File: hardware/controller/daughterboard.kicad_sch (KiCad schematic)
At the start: 9 parts, among them J1 TYPE-C-31-D-06, J8 FPC_12P_0.5mm, SW89 SW_Push, SW91 SW_Push, U3 TPD4E05U06DQAR

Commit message: feat(controller): 1x10 MB-DB header, isolate DB nets, drop DB buttons and LEDs
J9 (MB) and J8 (DB) as Conn_01x10 with I1 pinout; DB nets renamed DB_*,
no hierarchical links between MB and DB sheets; SW89, SW91, D4, D92 removed.
Layout around J9 still to be tidied.

Co-Authored-By: Claude Opus 5.5 (1M context) <noreply@anthropic.com>
Claude-Session: https://claude.ai/code/session_011u4PgyeeXFvTvHcxLBDiHw
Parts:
- removed D4, D92: rgb, easyeda2kicad:WS2812C-2020-V1, symbol easyeda2kicad:rgb
- removed SW89, SW91: SW_Push, easyeda2kicad:KEY-SMD_B3U-1000PM, symbol Switch:SW_Push
- J8: value FPC_12P_0.5mm -> J_DB 1x10 P1.00mm; footprint easyeda2kicad:FPC_12P_0.5mm -> Connector_PinHeader_1.00mm:PinHeader_1x10_P1.00mm_Vertical_SMD_Pin1Left; symbol Connector_Generic:Conn_01x12 -> Connector_Generic:Conn_01x10
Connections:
- net GND is gone; now on net DB_GND: D1.1 (A1), J1.A1 (GND), J1.A12 (GND), J1.B1 (GND), J1.B12 (GND), J1.S1 (SHIELD), J8.5 (Pin_5), J8.8 (Pin_8), U3.3 (GND), U3.8 (GND)
- net LED_DATA is gone; now on net DB_GND: J8.10 (Pin_10)
- net BT_PAIR renamed DB_GND
- net CC1 renamed DB_CC1
- net CC2 renamed DB_CC2
- net D+ renamed DB_D+
- net D- renamed DB_D-
- removed net SHPHLD: J8.11 (Pin_11)
- net VBUS renamed DB_VBUS
- removed net VSYS: J8.12 (Pin_12)
- no-connect marks 3 -> 2

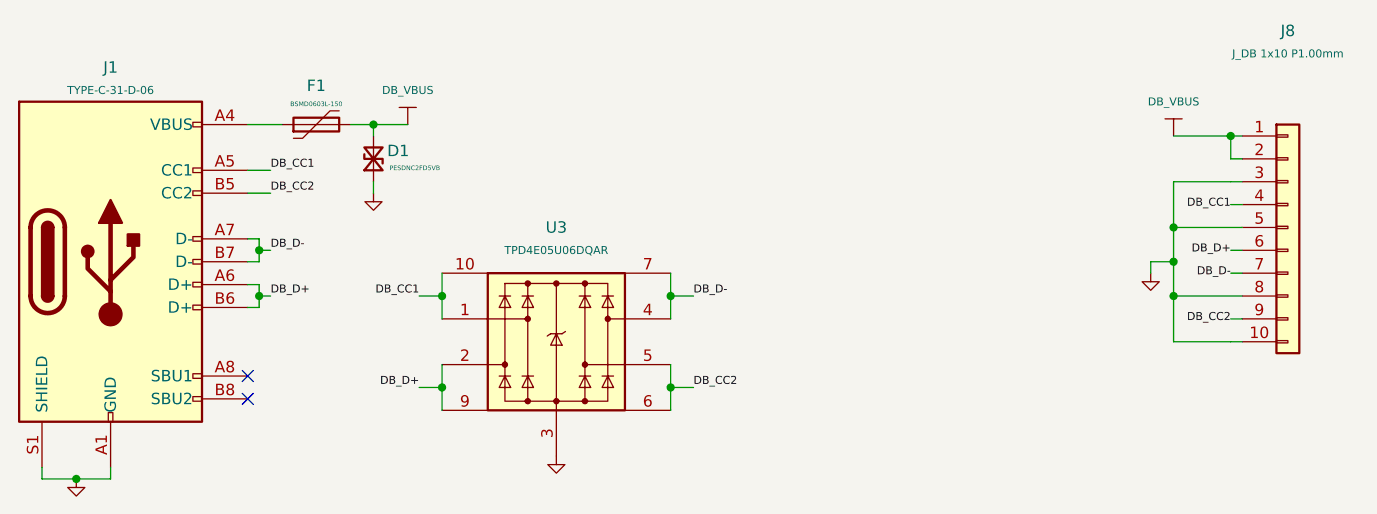
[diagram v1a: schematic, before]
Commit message: feat(controller): U2 on ibm_m nPM1300 symbol, PMIC step 1 (P1-P4, P7, P10)
BUCK2 drives VDD_NRF (L4 SW2-VOUT2, R10 470k on VSET2), BUCK1 terminated,
PVSS2 net-tie NT1 to GND, NTC to GND (TH1 removed), LSIN1 on VSYS,
VDDIO on VDD_NRF with C35 100n, GPIO0 PMIC_INT, GPIO1 LED_EN labels.

Co-Authored-By: Claude Opus 5.5 (1M context) <noreply@anthropic.com>
Claude-Session: https://claude.ai/code/session_011u4PgyeeXFvTvHcxLBDiHw
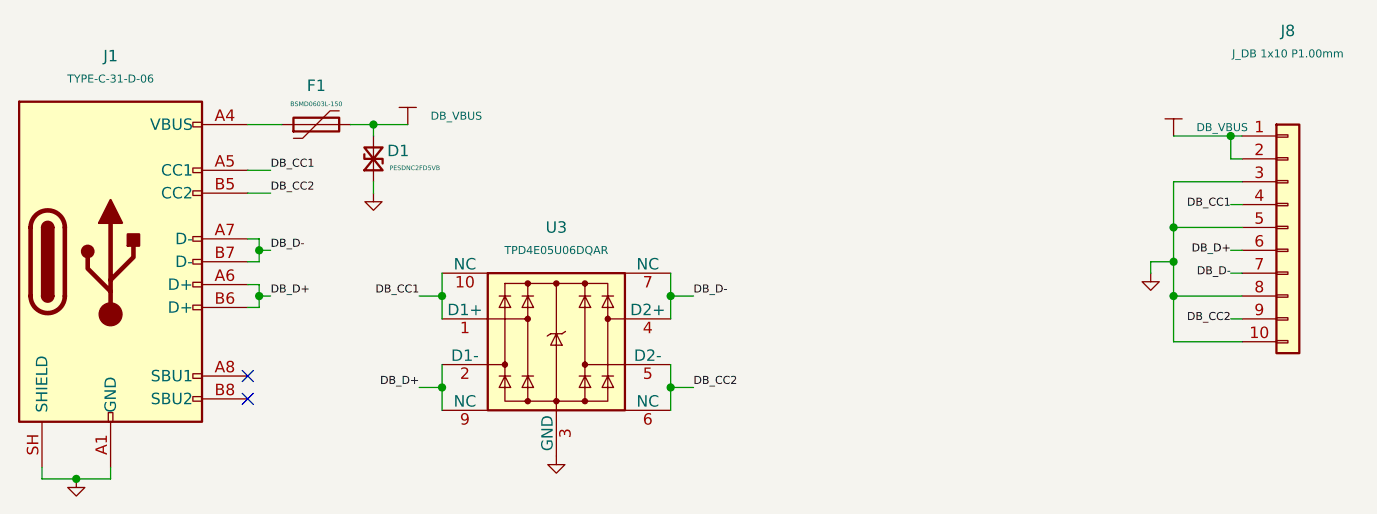
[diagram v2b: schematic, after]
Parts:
- D1: footprint easyeda2kicad:Diodes_DFN1006-2 -> (none); LCSC Part C110694 -> (none)
- F1: footprint Fuse:Fuse_0603_1608Metric -> (none); LCSC Part C914094 -> (none)
- J1: footprint easyeda2kicad:USB-C-SMD_TYPE-C-31-D-06 -> (none); LCSC Part C2689964 -> (none)
- J8: footprint Connector_PinHeader_1.00mm:PinHeader_1x10_P1.00mm_Vertical_SMD_Pin1Left -> (none); now in the parts list
- U3: LCSC Part C138714 -> (none)
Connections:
- net DB_GND: now also J1.SH (SHIELD); no longer J1.S1 (SHIELD)
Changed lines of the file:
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@@
+	)
+	(junction
+		(at 193.04 92.71)
+		(diameter 0)
+		(color 0 0 0 0)
+	)
+	(junction
+		(at 193.04 85.09)
+		(diameter 0)
+		(color 0 0 0 0)
 	)
 	(junction
@@
 	(wire
 		(pts
-			(xy 199.39 80.01) (xy 200.66 80.01)
+			(xy 193.04 80.01) (xy 200.66 80.01)
 		)
 		(stroke
@@
 	(wire
 		(pts
+			(xy 193.04 80.01) (xy 193.04 85.09)
+		)
+		(stroke
+			(width 0)
+			(type default)
+		)
+	)
+	(wire
+		(pts
 			(xy 200.66 77.47) (xy 199.39 77.47)
 		)
@@
 	(wire
 		(pts
+			(xy 193.04 92.71) (xy 193.04 97.79)
+		)
+		(stroke
+			(width 0)
+			(type default)
+		)
+	)
+	(wire
+		(pts
 			(xy 199.39 87.63) (xy 200.66 87.63)
 		)
@@
 	(wire
 		(pts
-			(xy 199.39 97.79) (xy 200.66 97.79)
-		)
-		(stroke
-			(width 0)
-			(type default)
-		)
-	)
-	(wire
-		(pts
 			(xy 101.6 73.66) (xy 104.14 73.66)
 		)
@@
 	(wire
 		(pts
+			(xy 193.04 97.79) (xy 200.66 97.79)
+		)
+		(stroke
+			(width 0)
+			(type default)
+		)
+	)
+	(wire
+		(pts
 			(xy 91.44 91.44) (xy 91.44 92.71)
 		)
@@
 			(width 0)
 			(type default)
+		)
+	)
+	(label "DB_CC2"
+		(at 199.39 95.25 180)
+		(effects
+			(font
+				(size 0.889 0.889)
+			)
+			(justify right)
+		)
+	)
+	(label "DB_D+"
+		(at 199.39 87.63 180)
+		(effects
+			(font
+				(size 0.889 0.889)
+			)
+			(justify right)
+		)
+	)
+	(label "DB_D-"
+		(at 199.39 90.17 180)
+		(effects
+			(font
+				(size 0.889 0.889)
+			)
+			(justify right)
+		)
+	)
+	(label "DB_CC1"
+		(at 199.39 82.55 180)
+		(effects
+			(font
+				(size 0.889 0.889)
+			)
+			(justify right)
 		)
 	)
@@
 			)
 			(justify left bottom)
-		)
-	)
-	(label "DB_CC2"
-		(at 199.39 95.25 180)
-		(effects
-			(font
-				(size 0.889 0.889)
-			)
-			(justify right)
-		)
-	)
-	(label "DB_D+"
-		(at 199.39 87.63 180)
-		(effects
-			(font
-				(size 0.889 0.889)
-			)
-			(justify right)
-		)
-	)
-	(label "DB_D-"
-		(at 199.39 90.17 180)
-		(effects
-			(font
-				(size 0.889 0.889)
-			)
-			(justify right)
-		)
-	)
-	(label "DB_CC1"
-		(at 199.39 82.55 180)
-		(effects
-			(font
-				(size 0.889 0.889)
-			)
-			(justify right)
 		)
 	)
@@
 			)
 		)
-		(property "Footprint" "Fuse:Fuse_0603_1608Metric"
+		(property "Footprint" ""
 			(at 102.87 72.39 0)
 			(hide yes)
@@
 			)
 		)
-		(property "Datasheet" "https://www.lcsc.com/product-detail/C914094.html"
+		(property "Datasheet" ""
 			(at 97.79 73.66 0)
 			(hide yes)
@@
 			)
 		)
-		(property "LCSC Part" "C914094"
-			(at 97.79 73.66 90)
-			(hide yes)
-			(show_name no)
-			(do_not_autoplace no)
-			(effects
-				(font
-					(size 1.27 1.27)
-				)
-			)
-		)
 		(pin "2"
 		)
@@
 		)
 		(instances
-			(project "ibm-modern-m-ssk"
+			(project "controller"
 				(path "/17f6a4a5-fbff-4e30-a1cc-9481373e4968/c9a46136-57a3-45fc-88ce-38da53378f82"
 					(reference "F1")
@@
 		)
 		(instances
-			(project "ibm-modern-m-ssk"
+			(project "controller"
 				(path "/17f6a4a5-fbff-4e30-a1cc-9481373e4968/c9a46136-57a3-45fc-88ce-38da53378f82"
 					(reference "#PWR037")
@@
 		(fields_autoplaced yes)
 		(property "Reference" "J1"
-			(at 74.93 67.31 0)
+			(at 74.93 66.04 0)
 			(show_name no)
 			(do_not_autoplace no)
@@
 		)
 		(property "Value" "TYPE-C-31-D-06"
-			(at 74.93 69.85 0)
+			(at 74.93 68.58 0)
 			(show_name no)
 			(do_not_autoplace no)
@@
 			)
 		)
-		(property "Footprint" "easyeda2kicad:USB-C-SMD_TYPE-C-31-D-06"
+		(property "Footprint" ""
 			(at 78.74 88.9 0)
 			(hide yes)
@@
 			)
 		)
-		(property "LCSC Part" "C2689964"
-			(at 74.93 88.9 0)
-			(hide yes)
-			(show_name no)
-			(do_not_autoplace no)
-			(effects
-				(font
-					(size 1.27 1.27)
-				)
-			)
-		)
-		(pin "S1"
+		(pin "SH"
 		)
 		(pin "B7"
@@
 		)
 		(instances
-			(project "ibm-modern-m-ssk"
+			(project "controller"
 				(path "/17f6a4a5-fbff-4e30-a1cc-9481373e4968/c9a46136-57a3-45fc-88ce-38da53378f82"
 					(reference "J1")
@@
 		(body_style 1)
 		(exclude_from_sim no)
-		(in_bom no)
+		(in_bom yes)
 		(on_board yes)
-		(in_pos_files no)
+		(in_pos_files yes)
 		(dnp no)
 		(property "Reference" "J8"
@@
 			)
 		)
-		(property "Footprint" "Connector_PinHeader_1.00mm:PinHeader_1x10_P1.00mm_Vertical_SMD_Pin1Left"
+		(property "Footprint" ""
 			(at 205.74 85.09 0)
 			(hide yes)
@@
 			)
 		)
-		(property "Datasheet" "~"
+		(property "Datasheet" ""
 			(at 205.74 85.09 0)
 			(hide yes)
@@
 			)
 		)
-		(property "Description" "Goldpin 1x10, raster 1,00 mm; lacze MB-DB, pinout wg I1: VBUS, VBUS, GND, CC1, GND, D+, D-, GND, CC2, GND. Strona DB: piny lutowane do krawedzi; footprint tymczasowy, poza BOM i CPL (czesc liczona przy J9)"
+		(property "Description" "Generic connector, single row, 01x10, script generated (kicad-library-utils/schlib/autogen/connector/)"
 			(at 205.74 85.09 0)
 			(hide yes)
@@
 			)
 		)
-		(property "LCSC Part" ""
-			(at 205.74 85.09 0)
-			(hide yes)
-			(show_name no)
-			(do_not_autoplace no)
-			(effects
-				(font
-					(size 1.27 1.27)
-				)
-			)
-		)
 		(pin "3"
 		)
@@
 		)
 		(instances
-			(project "ibm-modern-m-ssk"
+			(project "controller"
 				(path "/17f6a4a5-fbff-4e30-a1cc-9481373e4968/c9a46136-57a3-45fc-88ce-38da53378f82"
 					(reference "J8")
@@
 			)
 		)
-		(property "Footprint" "easyeda2kicad:Diodes_DFN1006-2"
+		(property "Footprint" ""
 			(at 104.14 77.47 0)
 			(hide yes)
@@
 			)
 		)
-		(property "Datasheet" "https://www.lcsc.com/product-detail/C110694.html"
+		(property "Datasheet" ""
 			(at 104.14 77.47 0)
 			(hide yes)
@@
 			)
 		)
-		(property "LCSC Part" "C110694"
-			(at 104.14 77.47 90)
-			(hide yes)
-			(show_name no)
-			(do_not_autoplace no)
-			(effects
-				(font
-					(size 1.27 1.27)
-				)
-			)
-		)
 		(pin "1"
 		)
@@
 		)
 		(instances
-			(project "ibm-modern-m-ssk"
+			(project "controller"
 				(path "/17f6a4a5-fbff-4e30-a1cc-9481373e4968/c9a46136-57a3-45fc-88ce-38da53378f82"
 					(reference "D1")
@@
 			)
 		)
-		(property "LCSC Part" "C138714"
-			(at 124.46 97.79 0)
-			(hide yes)
-			(show_name no)
-			(do_not_autoplace no)
-			(effects
-				(font
-					(size 1.27 1.27)
-				)
-			)
-		)
 		(pin "5"
 		)
@@
 		)
 		(instances
-			(project "ibm-modern-m-ssk"
+			(project "controller"
 				(path "/17f6a4a5-fbff-4e30-a1cc-9481373e4968/c9a46136-57a3-45fc-88ce-38da53378f82"
 					(reference "U3")
@@
 		)
 		(instances
-			(project "ibm-modern-m-ssk"
+			(project "controller"
 				(path "/17f6a4a5-fbff-4e30-a1cc-9481373e4968/c9a46136-57a3-45fc-88ce-38da53378f82"
 					(reference "#PWR038")
@@
 		)
 		(property "Value" "DB_VBUS"
-			(at 107.95 69.85 0)
+			(at 110.49 72.7075 0)
 			(show_name no)
 			(do_not_autoplace no)
@@
 					(size 0.889 0.889)
 				)
+				(justify left)
 			)
 		)
@@
 		)
 		(instances
-			(project "ibm-modern-m-ssk"
+			(project "controller"
 				(path "/17f6a4a5-fbff-4e30-a1cc-9481373e4968/c9a46136-57a3-45fc-88ce-38da53378f82"
 					(reference "#LABEL05")
@@
 		)
 		(instances
-			(project "ibm-modern-m-ssk"
+			(project "controller"
 				(path "/17f6a4a5-fbff-4e30-a1cc-9481373e4968/c9a46136-57a3-45fc-88ce-38da53378f82"
 					(reference "#PWR039")
@@
 		)
 		(property "Value" "DB_VBUS"
-			(at 193.04 71.12 0)
+			(at 195.58 73.9775 0)
 			(show_name no)
 			(do_not_autoplace no)
@@
 					(size 0.889 0.889)
 				)
+				(justify left)
 			)
 		)
@@
 		)
 		(instances
-			(project "ibm-modern-m-ssk"
+			(project "controller"
 				(path "/17f6a4a5-fbff-4e30-a1cc-9481373e4968/c9a46136-57a3-45fc-88ce-38da53378f82"
 					(reference "#LABEL032")
@@
 		)
 		(instances
-			(project "ibm-modern-m-ssk"
+			(project "controller"
 				(path "/17f6a4a5-fbff-4e30-a1cc-9481373e4968/c9a46136-57a3-45fc-88ce-38da53378f82"
 					(reference "#PWR040")
@@
 		)
 	)
-	(wire
-		(pts
-			(xy 193.04 80.01) (xy 199.39 80.01)
-		)
-		(stroke
-			(width 0)
-			(type default)
-		)
-	)
-	(wire
-		(pts
-			(xy 193.04 80.01) (xy 193.04 85.09)
-		)
-		(stroke
-			(width 0)
-			(type default)
-		)
-	)
-	(wire
-		(pts
-			(xy 193.04 97.79) (xy 199.39 97.79)
-		)
-		(stroke
-			(width 0)
-			(type default)
-		)
-	)
-	(wire
-		(pts
-			(xy 193.04 92.71) (xy 193.04 97.79)
-		)
-		(stroke
-			(width 0)
-			(type default)
-		)
-	)
-	(junction
-		(at 193.04 85.09)
-		(diameter 0)
-		(color 0 0 0 0)
-	)
-	(junction
-		(at 193.04 92.71)
-		(diameter 0)
-		(color 0 0 0 0)
-	)
 )

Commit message: fix(controller): restore footprints and LCSC fields lost on symbol update; PMIC P5, S2, P8, P9
Footprint and LCSC Part restored from 6fba3e8 for every symbol whose value
is unchanged (MB and DB); J8/J9 descriptions restored. Q1 (now AO3401A)
left for manual footprint assignment.

Co-Authored-By: Claude Opus 5.5 (1M context) <noreply@anthropic.com>
Claude-Session: https://claude.ai/code/session_011u4PgyeeXFvTvHcxLBDiHw
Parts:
- D1: footprint (none) -> easyeda2kicad:Diodes_DFN1006-2; LCSC Part (none) -> C110694
- F1: footprint (none) -> Fuse:Fuse_0603_1608Metric; LCSC Part (none) -> C914094
- J1: footprint (none) -> easyeda2kicad:USB-C-SMD_TYPE-C-31-D-06; LCSC Part (none) -> C2689964
- J8: footprint (none) -> Connector_PinHeader_1.00mm:PinHeader_1x10_P1.00mm_Vertical_SMD_Pin1Left
- U3: LCSC Part (none) -> C138714
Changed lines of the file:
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@@
 			)
 		)
-		(property "Footprint" ""
+		(property "Footprint" "Fuse:Fuse_0603_1608Metric"
 			(at 102.87 72.39 0)
 			(hide yes)
@@
 		(property "Description" "Resettable fuse, polymeric positive temperature coefficient"
 			(at 97.79 73.66 0)
+			(hide yes)
+			(show_name no)
+			(do_not_autoplace no)
+			(effects
+				(font
+					(size 1.27 1.27)
+				)
+			)
+		)
+		(property "LCSC Part" "C914094"
+			(at 97.79 73.66 90)
 			(hide yes)
 			(show_name no)
@@
 			)
 		)
-		(property "Footprint" ""
+		(property "Footprint" "easyeda2kicad:USB-C-SMD_TYPE-C-31-D-06"
 			(at 78.74 88.9 0)
 			(hide yes)
@@
 		)
 		(property "Description" "USB 2.0-only 16P Type-C Receptacle connector"
+			(at 74.93 88.9 0)
+			(hide yes)
+			(show_name no)
+			(do_not_autoplace no)
+			(effects
+				(font
+					(size 1.27 1.27)
+				)
+			)
+		)
+		(property "LCSC Part" "C2689964"
 			(at 74.93 88.9 0)
 			(hide yes)
@@
 			)
 		)
-		(property "Footprint" ""
+		(property "Footprint" "Connector_PinHeader_1.00mm:PinHeader_1x10_P1.00mm_Vertical_SMD_Pin1Left"
 			(at 205.74 85.09 0)
 			(hide yes)
@@
 			)
 		)
-		(property "Description" "Generic connector, single row, 01x10, script generated (kicad-library-utils/schlib/autogen/connector/)"
+		(property "Description" "Goldpin 1x10, raster 1,00 mm; lacze MB-DB, pinout wg I1: VBUS, VBUS, GND, CC1, GND, D+, D-, GND, CC2, GND. Strona DB: piny lutowane do krawedzi; footprint tymczasowy, poza BOM i CPL (czesc liczona przy J9)"
 			(at 205.74 85.09 0)
 			(hide yes)
@@
 			)
 		)
-		(property "Footprint" ""
+		(property "Footprint" "easyeda2kicad:Diodes_DFN1006-2"
 			(at 104.14 77.47 0)
 			(hide yes)
@@
 		(property "Description" "Bidirectional transient-voltage-suppression diode, small symbol"
 			(at 104.14 77.47 0)
+			(hide yes)
+			(show_name no)
+			(do_not_autoplace no)
+			(effects
+				(font
+					(size 1.27 1.27)
+				)
+			)
+		)
+		(property "LCSC Part" "C110694"
+			(at 104.14 77.47 90)
 			(hide yes)
 			(show_name no)
@@
 			(at 124.46 97.79 0)
 			(hide yes)
+			(show_name no)
+			(do_not_autoplace no)
+			(effects
+				(font
+					(size 1.27 1.27)
+				)
+			)
+		)
+		(property "LCSC Part" "C138714"
+			(at 124.46 97.79 0)
+			(hide yes)
